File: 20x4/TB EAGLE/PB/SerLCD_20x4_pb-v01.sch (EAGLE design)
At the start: 19 parts, among them J1 AVR_PROG, J3 SER_LCD20X4, U1 5V Flying Jalapeno, U2 74LVC4066_MUX_1:1_X4

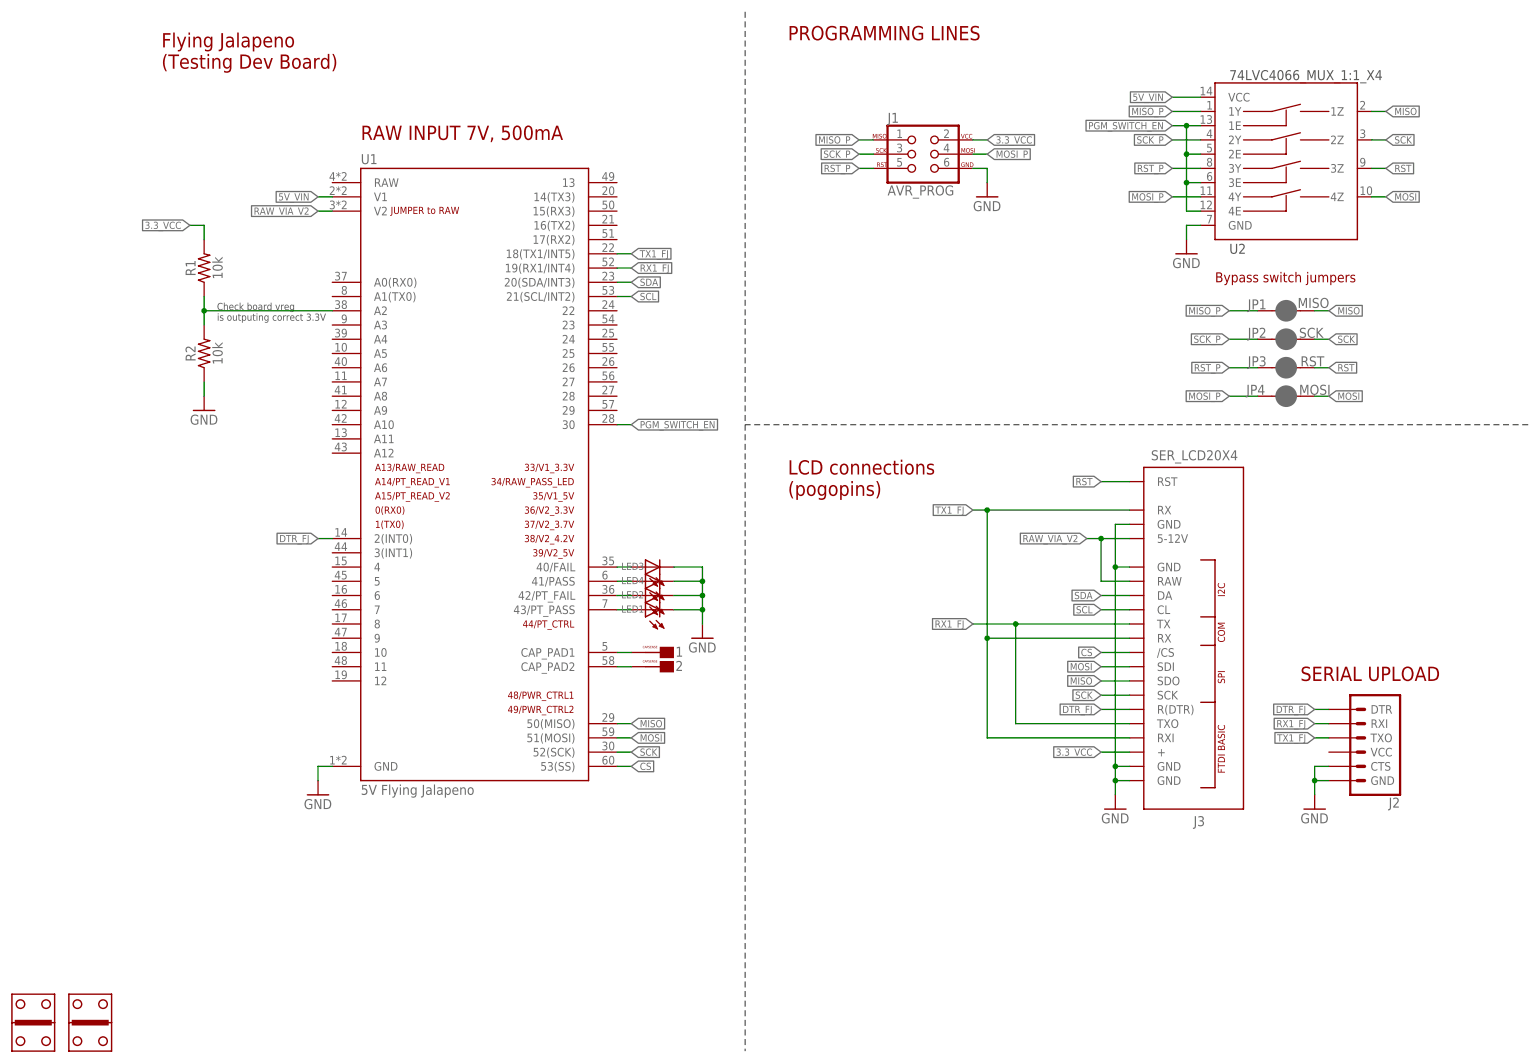
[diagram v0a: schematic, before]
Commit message: added preTest to 3.3V output on 20x4
ready to order both designs... gonna throw on a QC panel asap
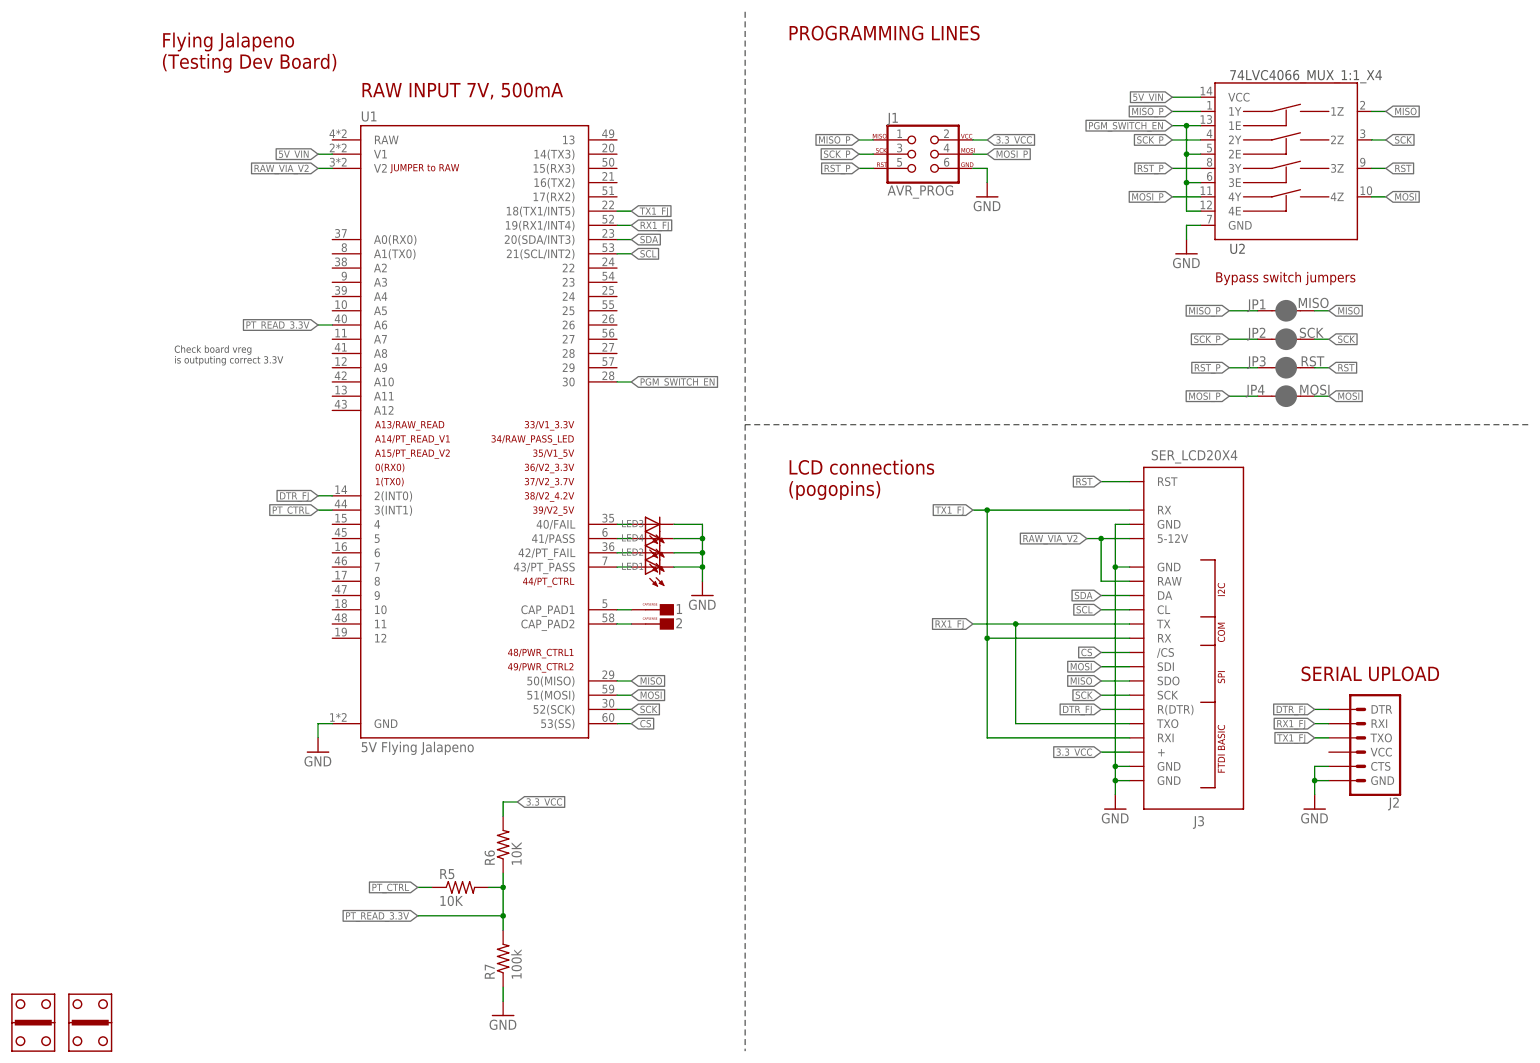
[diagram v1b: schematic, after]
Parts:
- removed R1, R2: 10k, SparkFun-Resistors:10KOHM-0603-1/10W-1%
- added R5, R6: 10K, SparkFun-Resistors:10KOHM1/10W1%(0603)0603
- added R7: 100k, SparkFun-Resistors:100KOHM1/10W1%(0603)
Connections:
- removed net N$7: R1.1, R2.2, U1.A2
- new net PT_CTRL: R5.1, U1.3(INT1)
- new net PT_READ_3.3V: R5.2, R6.1, R7.2, U1.A6
- net 3.3_VCC: now also R6.2; no longer R1.2
- net GND: now also R7.1; no longer R2.1
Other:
- moved on the sheet: 1, 2, LED1, LED2, LED3, LED4, U1
